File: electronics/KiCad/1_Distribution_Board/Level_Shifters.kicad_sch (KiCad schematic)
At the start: 25 parts, among them J10 Generic 2.54mm, J11 Generic 2.54mm, J5 Generic 2.54mm, J8 Generic 2.54mm, J9 Generic 2.54mm, Q2 AO3400A, Q3 AO3400A, Q4 AO3400A, Q5 AO3400A, Q6 BSS138

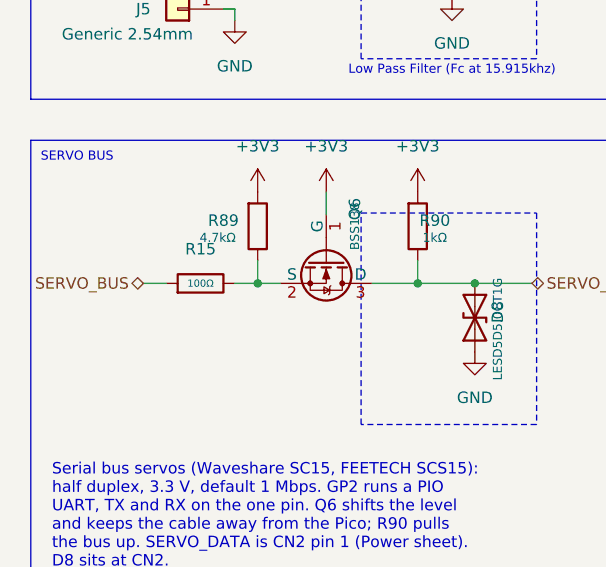
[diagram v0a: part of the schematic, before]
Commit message: distribution board v1.5: R15 0 ohm so the servo bus low meets Feetech's 0.45 V
Feetech's bus servos specify their signal low as 0 to 0.45 V. With R90
(1k to 3.3 V) and R89 (4.7k) on the line, about 3.4 mA flows through
R15 whenever the Pico holds the bus low, so its 100 ohm added 0.34 V
on top of the Pico's output low and the estimate at the servo was 0.63
to 0.81 V. R15 came from the earlier board, where GP2 drove the cable
directly; here Q6 already isolates GP2 from the cable. With 0 ohm the
low is the Pico's VOL plus Q6, about 0.2 V at 12 mA drive strength.
Firmware must drive GP2 open-drain (low or released, never high while
a servo can answer), since R15 no longer limits contention current.

Value and part only (0603WAF0000T5E, LCSC C21189, basic): footprint,
placement and copper are unchanged. DRC, ERC and parity as before.

Co-Authored-By: Claude Opus 5.5 <noreply@anthropic.com>
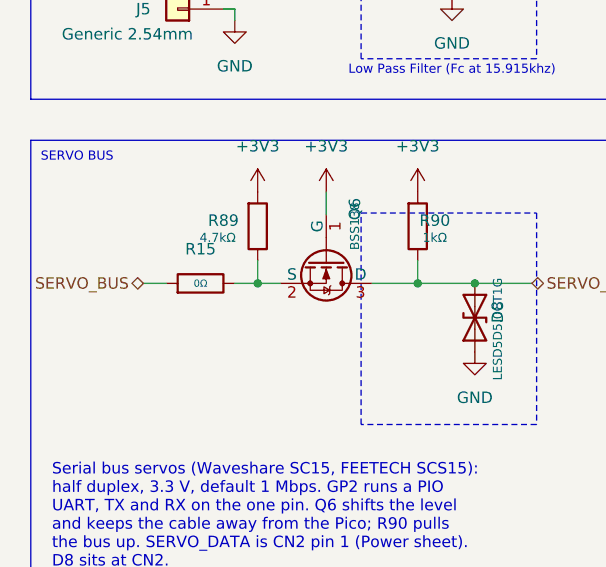
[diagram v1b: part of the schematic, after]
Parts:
- R15: value 100Ω -> 0Ω; symbol PCM_JLCPCB-Resistors:0603,100Ω -> PCM_JLCPCB-Resistors:0603,0Ω; LCSC C22775 -> C21189; Part 0603WAF1000T5E -> 0603WAF0000T5E; Price 0.004USD -> (none); Resistance 100Ω -> 0Ω; Stock 8202320 -> (none)
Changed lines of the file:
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@@
 	)
 	(symbol
-		(lib_id "PCM_JLCPCB-Resistors:0603,100Ω")
+		(lib_id "PCM_JLCPCB-Resistors:0603,0Ω")
 		(at 36.83 82.55 90)
 		(unit 1)
@@
 			)
 		)
-		(property "Value" "100Ω"
+		(property "Value" "0Ω"
 			(at 36.83 82.55 90)
 			(show_name no)
@@
 			)
 		)
-		(property "Description" "100mW Thick Film Resistors 75V ±1% ±200ppm/°C 100Ω 0603 Chip Resistor - Surface Mount ROHS"
+		(property "Description" "Jumper 0Ω 0603 Chip Resistor - Surface Mount"
 			(at 36.83 82.55 0)
 			(hide yes)
@@
 			)
 		)
-		(property "LCSC" "C22775"
+		(property "LCSC" "C21189"
 			(at 36.83 82.55 0)
 			(hide yes)
@@
 			)
 		)
-		(property "Stock" "8202320"
+		(property "Stock" ""
 			(at 36.83 82.55 0)
 			(hide yes)
@@
 			)
 		)
-		(property "Price" "0.004USD"
+		(property "Price" ""
 			(at 36.83 82.55 0)
 			(hide yes)
@@
 			)
 		)
-		(property "Part" "0603WAF1000T5E"
+		(property "Part" "0603WAF0000T5E"
 			(at 36.83 82.55 0)
 			(hide yes)
@@
 			)
 		)
-		(property "Resistance" "100Ω"
+		(property "Resistance" "0Ω"
 			(at 36.83 82.55 0)
 			(hide yes)

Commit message: distribution board v1.5: LED port clamps, GP7 pull-up, low-ESR bulk caps
- D12-D15 (BAS316) from each LED port's switched side to +24V, so an
  inductive load (a fan, a long lead) cannot push the 30 V AO3400A
  switches past their rating at turn-off. A silicon diode rather than a
  Schottky: these sit at 24 V reverse whenever their port is on, and a
  small Schottky's leakage can heat it into thermal runaway. BAS316 is
  rated 30 uA at 25 V with a 150 C junction.
- R105 (10k) pulls GP7, the Pico's TX to the Pi through the isolator, up
  to 3.3 V. The RP2040 holds its pins low through reset, which reached
  the Pi's RX as a break.
- C11-C15 become Panasonic EEE-FT1V101AP (0.26 ohm ESR and 300 mA ripple
  at 100 kHz) on the same footprint; the previous part gave no ESR.
- The isolated ground island ends 0.25 mm sooner, so the Pi side keeps
  1 mm from the board's copper (it was 0.88 mm at J36), with one via to
  keep the island's front fill joined.
- GP19 under U8 moves to the back layer so U8's ground pin stays joined
  to the pour.
- D11-D15 silkscreen lines are 0.15 mm.

Co-Authored-By: Claude Opus 5.5 <noreply@anthropic.com>
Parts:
- added D12, D13, D14, D15: BAS316, Diode_SMD:D_SOD-323, symbol Device:D
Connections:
- net +24V: now also D12.1 (K), D13.1 (K), D14.1 (K), D15.1 (K)
- net at J8.2 (Pin_2), Q2.3 (D): now also D12.2 (A)
- net at J9.2 (Pin_2), Q3.3 (D): now also D13.2 (A)
- net at J11.2 (Pin_2), Q5.3 (D): now also D15.2 (A)
- net at J10.2 (Pin_2), Q4.3 (D): now also D14.2 (A)
